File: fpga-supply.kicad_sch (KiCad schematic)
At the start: 167 parts, among them J19 15910060, J20 15910060, U1 XC7K410T-2FFG900I

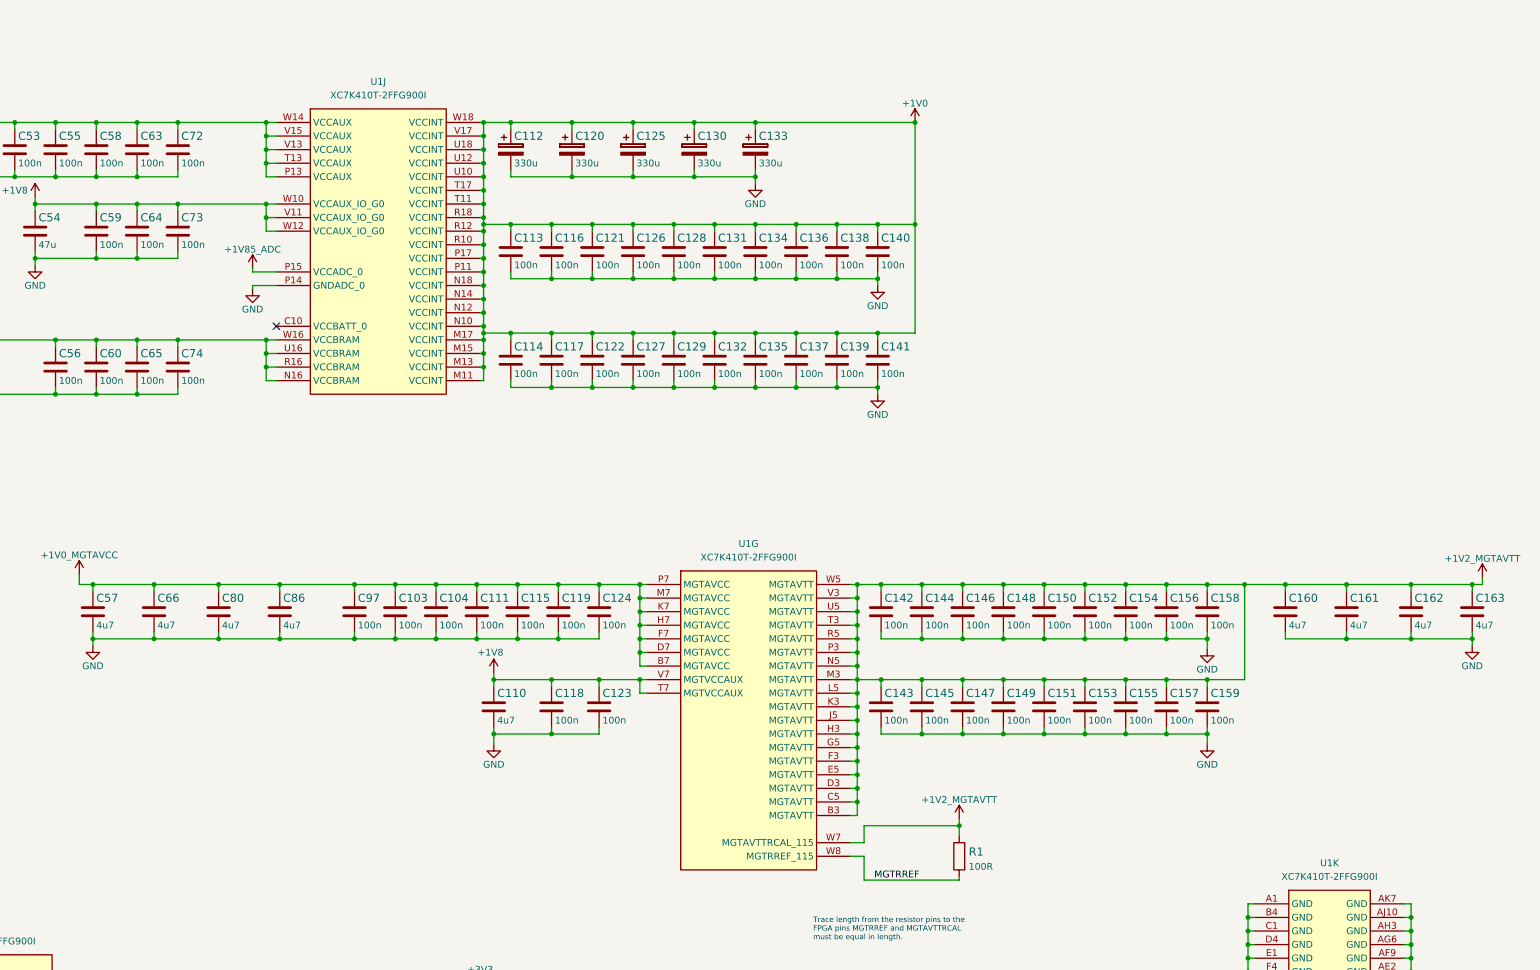
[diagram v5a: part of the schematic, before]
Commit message: Finish placing the decoulplig under FPGA, adjust power planes, color voltage domains
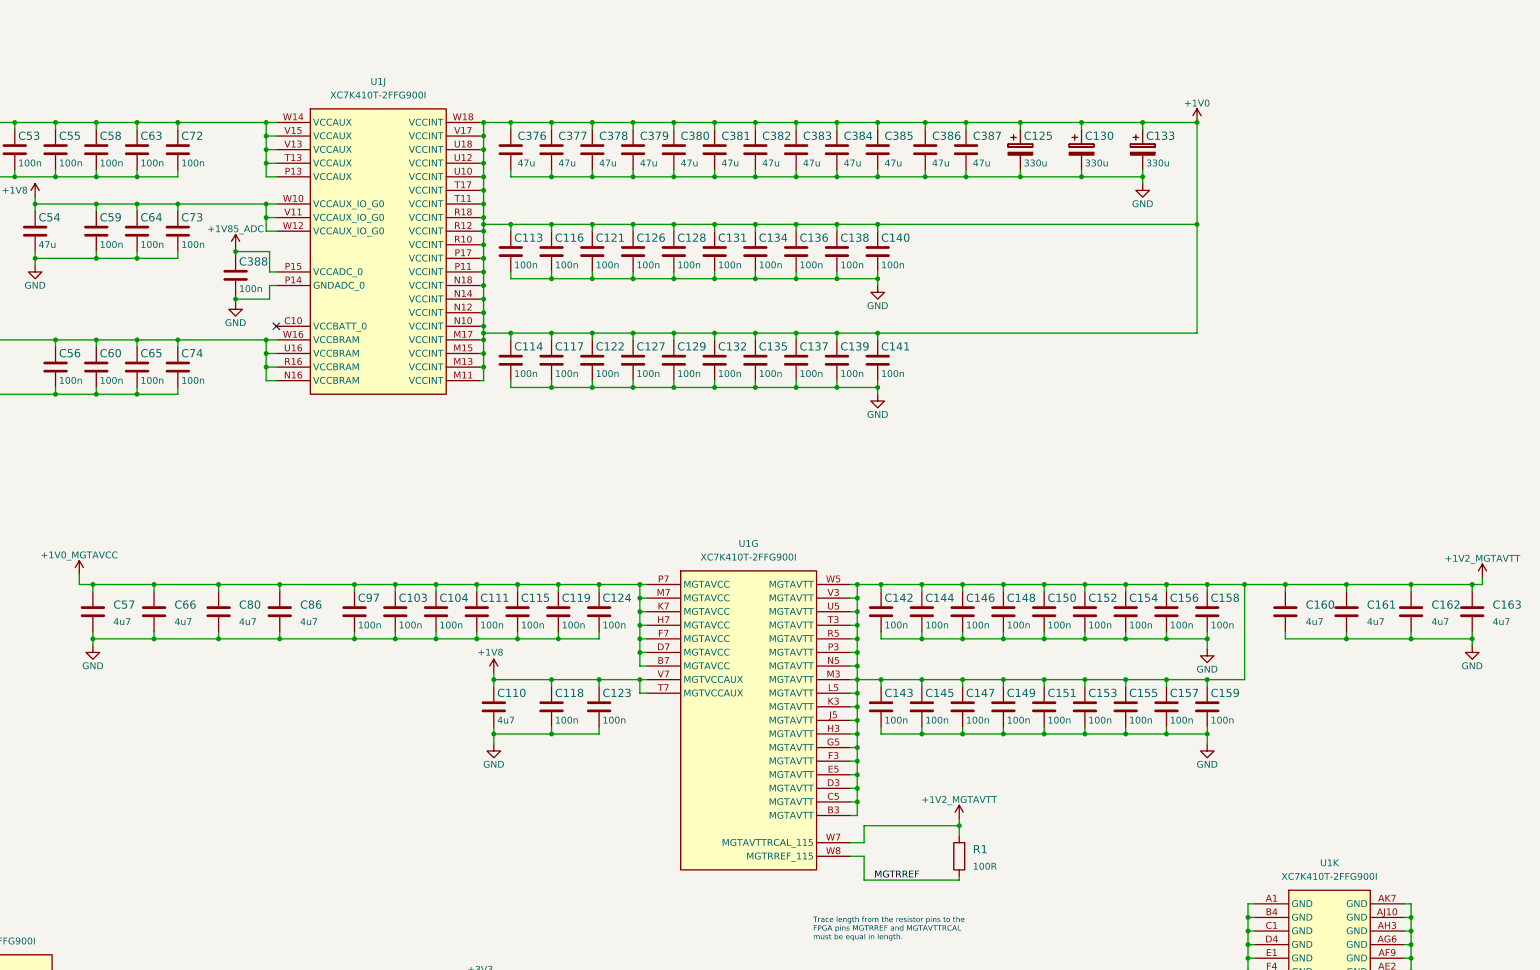
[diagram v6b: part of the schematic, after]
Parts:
- removed C112, C120: C_330u_KEMET_B, antmicro-footprints:KEMET_B, symbol antmicroCapacitorspol:C_330u_KEMET_B
- removed C160, C161, C162, C163, C57, C66, C80, C86: C_4u7_0402, antmicro-footprints:0402-cap, symbol antmicroCapacitors0402:C_4u7_0402
- removed R1: R_100R_0402, antmicro-footprints:0402-res, symbol antmicroResistors0402:R_100R_0402
- added C160, C161, C162, C163, C57, C66, C80, C86: C_4u7_0201, antmicro-footprints:0201-res, symbol antmicroCapacitorsmisc:C_4u7_0201
- added C376, C377, C378, C379, C380, C381, C382, C383, C384, C385, C386, C387: C_47u_0603, antmicro-footprints:0603-cap, symbol antmicroCapacitors0603:C_47u_0603
- added C388: C_100n_0201, antmicro-footprints:0201-res, symbol antmicroCapacitorsmisc:C_100n_0201
- added R1: R_100R_0201, antmicro-footprints:0201-res, symbol antmicroResistorsmisc:R_100R_0201
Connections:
- net +1V0: now also C376.1, C377.1, C378.1, C379.1, C380.1, C381.1, C382.1, C383.1, C384.1, C385.1, C386.1, C387.1
- net +1V0_MGTAVCC: now also C57.1, C66.1, C80.1, C86.1
- net +1V2_MGTAVTT: now also C160.1, C161.1, C162.1, C163.1, R1.2
- net +1V85_ADC: now also C388.1
- net GND: now also C160.2, C161.2, C162.2, C163.2, C376.2, C377.2, C378.2, C379.2, C380.2, C381.2, C382.2, C383.2, C384.2, C385.2, C386.2, C387.2, C388.2, C57.2, C66.2, C80.2, C86.2
- net MGTRREF: now also R1.1
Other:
- moved on the sheet: C125, C130, C133

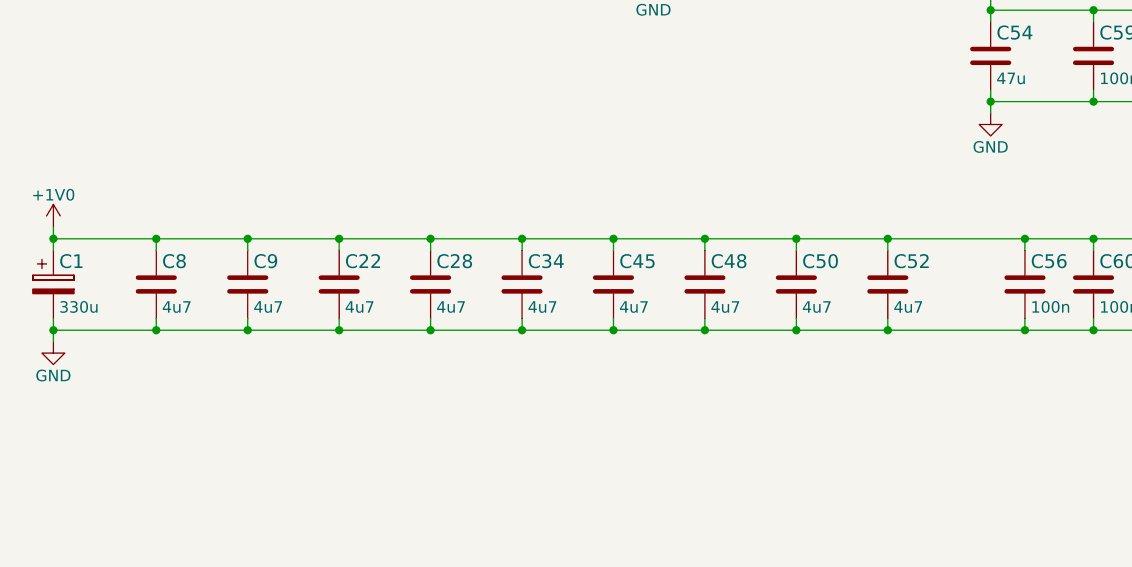
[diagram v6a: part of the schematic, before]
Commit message: Replace BRAM 4u7 caps to 0201, optimize decoupling placement
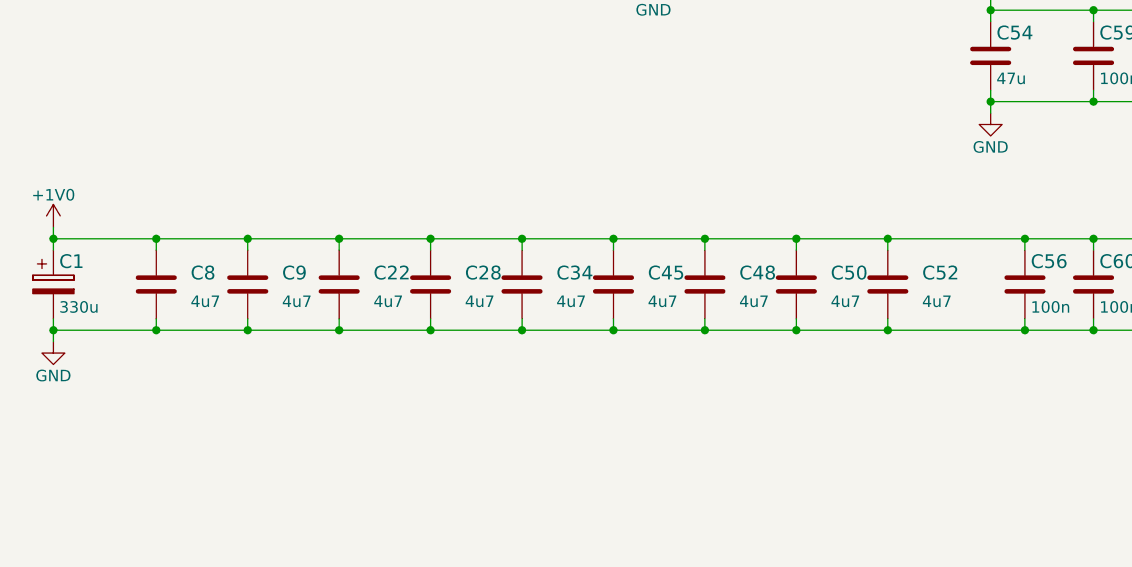
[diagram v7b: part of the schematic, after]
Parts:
- removed C22, C28, C34, C45, C48, C50, C52, C8, C9: C_4u7_0402, antmicro-footprints:0402-cap, symbol antmicroCapacitors0402:C_4u7_0402
- added C22, C28, C34, C45, C48, C50, C52, C8, C9: C_4u7_0201, antmicro-footprints:0201-res, symbol antmicroCapacitorsmisc:C_4u7_0201
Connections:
- net +1V0: now also C22.1, C28.1, C34.1, C45.1, C48.1, C50.1, C52.1, C8.1, C9.1
- net GND: now also C22.2, C28.2, C34.2, C45.2, C48.2, C50.2, C52.2, C8.2, C9.2

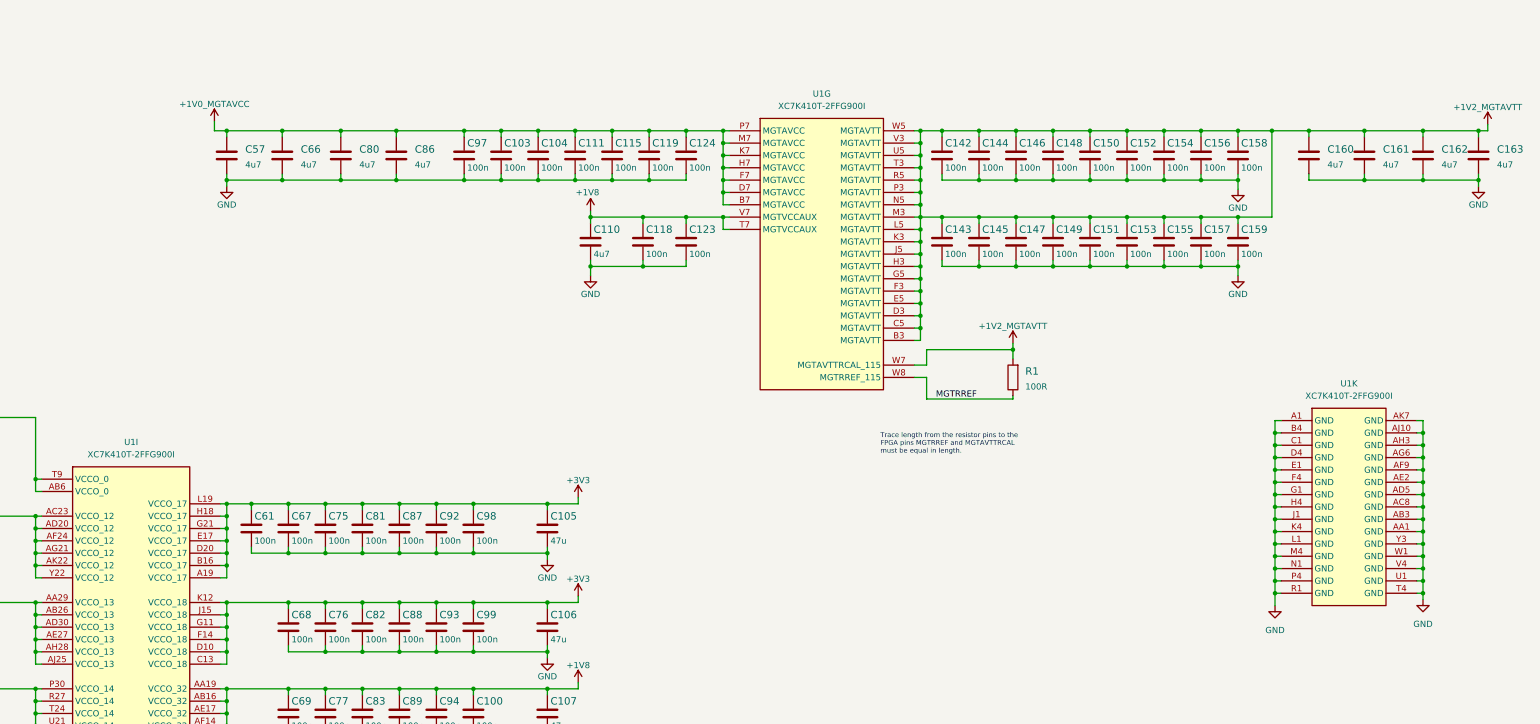
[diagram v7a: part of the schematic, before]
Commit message: Replace 3D model for 0201 capacitors, Add decoupling capacitors for MGT transcivers, flip MGT fanout, finish decoupling
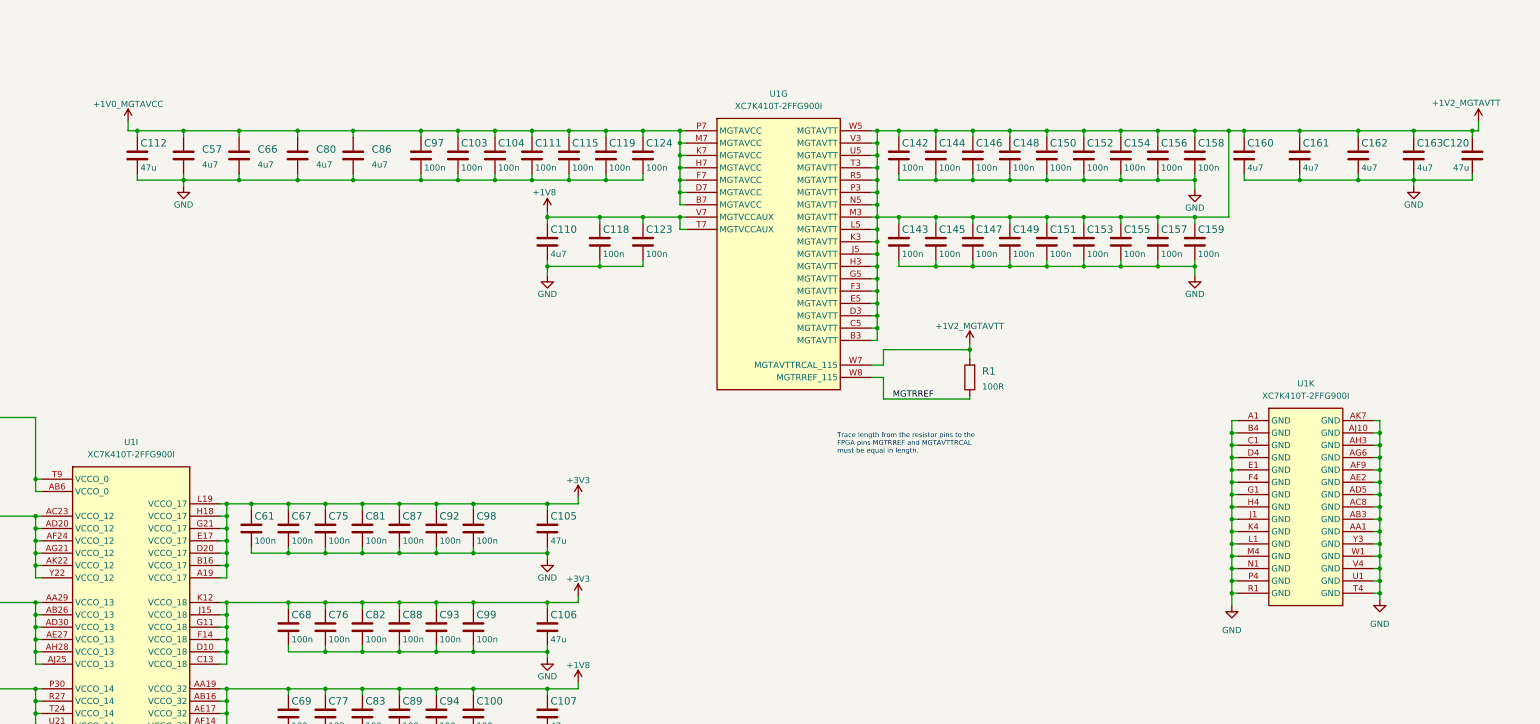
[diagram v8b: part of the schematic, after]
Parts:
- added C112, C120: C_47u_0603, antmicro-footprints:0603-cap, symbol antmicroCapacitors0603:C_47u_0603
- C160, C161, C162, C163, C22, C28, C34, C45, C48, C50, C52, C57, C66, C8, C80, C86, C9: MPN GRM035R60J475ME15D -> GRM035R60J475ME15D
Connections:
- net +1V0_MGTAVCC: now also C112.1
- net +1V2_MGTAVTT: now also C120.1
- net GND: now also C112.2, C120.2
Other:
- moved on the sheet: C103, C104, C110, C111, C115, C118, C119, C123, C124, C142, C143, C144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
